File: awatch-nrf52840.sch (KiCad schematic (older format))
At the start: 24 parts, among them U1 nRF52840, X1 ABM11W-32.0000MHZ-8-B1U-T3

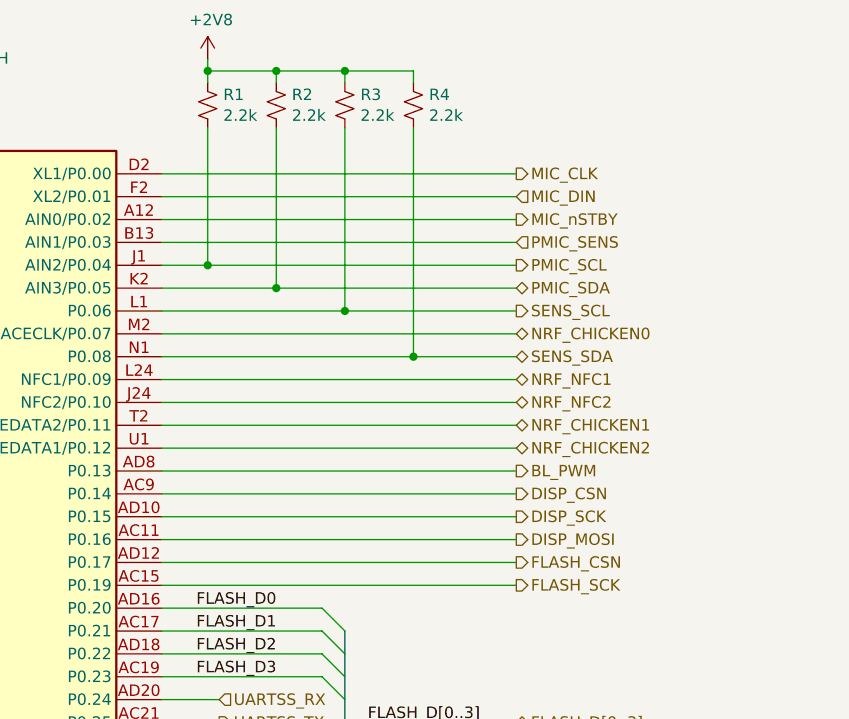
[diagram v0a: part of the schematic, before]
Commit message: route NFC
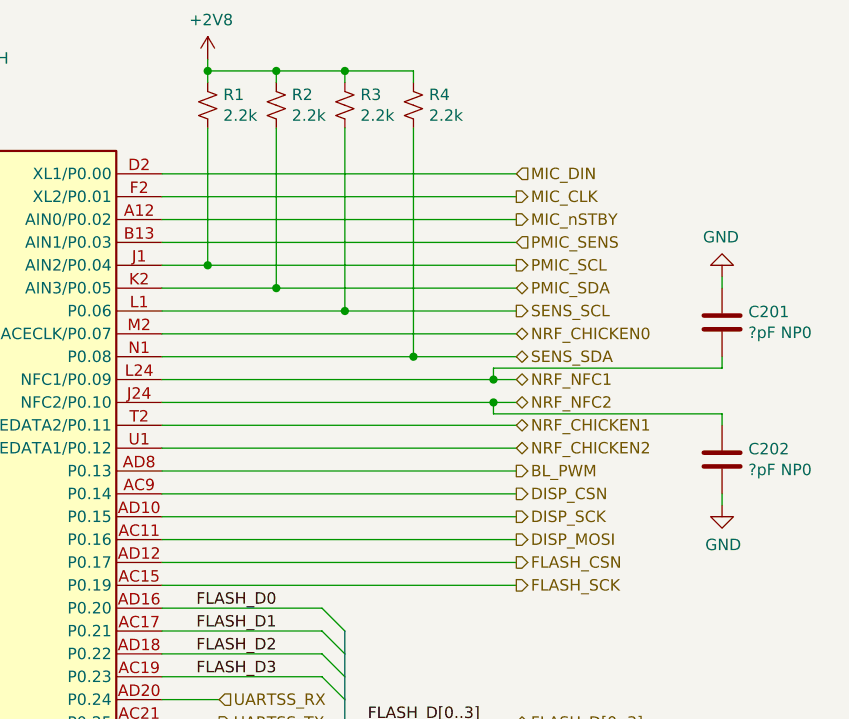
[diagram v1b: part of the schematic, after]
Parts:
- added C201, C202: ?pF NP0, Capacitor_SMD:C_0603_1608Metric, symbol Device:C
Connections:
- net GND: now also C201.1, C202.2
- net MIC_CLK: now also U1.F2 (XL2/P0.01); no longer U1.D2 (XL1/P0.00)
- net MIC_DIN: now also U1.D2 (XL1/P0.00); no longer U1.F2 (XL2/P0.01)
- net NRF_NFC1: now also C201.2
- net NRF_NFC2: now also C202.1
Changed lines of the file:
@@
 Wire Wire Line
 	6700 2100 5150 2100
-Text HLabel 6700 2000 2    50   Output ~ 0
+Text HLabel 6700 2100 2    50   Output ~ 0
 MIC_CLK
-Text HLabel 6700 2100 2    50   Input ~ 0
+Text HLabel 6700 2000 2    50   Input ~ 0
 MIC_DIN
 Text HLabel 6700 2200 2    50   Output ~ 0
@@
 NRF_NFC2
 Wire Wire Line
-	6700 3000 5150 3000
-Wire Wire Line
-	5150 2900 6700 2900
+	6700 3000 6600 3000
+Wire Wire Line
+	5150 2900 6600 2900
 Text HLabel 6700 2700 2    50   BiDi ~ 0
 NRF_CHICKEN0
@@
 	1900 2700 2050 2700
 $Comp
-L power:GND #PWR?
+L power:GND #PWR0141
 U 1 1 5C322A37
 P 1900 3100
-F 0 "#PWR?" H 1900 2850 50  0001 C CNN
+F 0 "#PWR0141" H 1900 2850 50  0001 C CNN
 F 1 "GND" H 1905 2927 50  0000 C CNN
 F 2 "" H 1900 3100 50  0001 C CNN
@@
 Wire Wire Line
 	1900 3000 1900 3100
+$Comp
+L Device:C C201
+U 1 1 5C3ACC54
+P 7600 2650
+F 0 "C201" H 7715 2696 50  0000 L CNN
+F 1 "?pF NP0" H 7715 2605 50  0000 L CNN
+F 2 "Capacitor_SMD:C_0603_1608Metric" H 7638 2500 50  0001 C CNN
+F 3 "~" H 7600 2650 50  0001 C CNN
+	1    7600 2650
+	1    0    0    -1
+$EndComp
+$Comp
+L Device:C C202
+U 1 1 5C3ACCC4
+P 7600 3250
+F 0 "C202" H 7715 3296 50  0000 L CNN
+F 1 "?pF NP0" H 7715 3205 50  0000 L CNN
+F 2 "Capacitor_SMD:C_0603_1608Metric" H 7638 3100 50  0001 C CNN
+F 3 "~" H 7600 3250 50  0001 C CNN
+	1    7600 3250
+	1    0    0    -1
+$EndComp
+Wire Wire Line
+	6600 2900 6600 2850
+Wire Wire Line
+	6600 2850 7600 2850
+Connection ~ 6600 2900
+Wire Wire Line
+	6600 2900 6700 2900
+Wire Wire Line
+	6600 3000 6600 3050
+Wire Wire Line
+	6600 3050 7600 3050
+Connection ~ 6600 3000
+Wire Wire Line
+	6600 3000 5150 3000
+$Comp
+L power:GND #PWR0209
+U 1 1 5C3B6652
+P 7600 3450
+F 0 "#PWR0209" H 7600 3200 50  0001 C CNN
+F 1 "GND" H 7605 3277 50  0000 C CNN
+F 2 "" H 7600 3450 50  0001 C CNN
+F 3 "" H 7600 3450 50  0001 C CNN
+	1    7600 3450
+	1    0    0    -1
+$EndComp
+$Comp
+L power:GND #PWR0208
+U 1 1 5C3BB5DC
+P 7600 2450
+F 0 "#PWR0208" H 7600 2200 50  0001 C CNN
+F 1 "GND" H 7605 2277 50  0000 C CNN
+F 2 "" H 7600 2450 50  0001 C CNN
+F 3 "" H 7600 2450 50  0001 C CNN
+	1    7600 2450
+	-1   0    0    1
+$EndComp
+Wire Wire Line
+	7600 3400 7600 3450
+Wire Wire Line
+	7600 3100 7600 3050
+Wire Wire Line
+	7600 2450 7600 2500
+Wire Wire Line
+	7600 2800 7600 2850
 Wire Bus Line
 	5950 4000 5950 4400

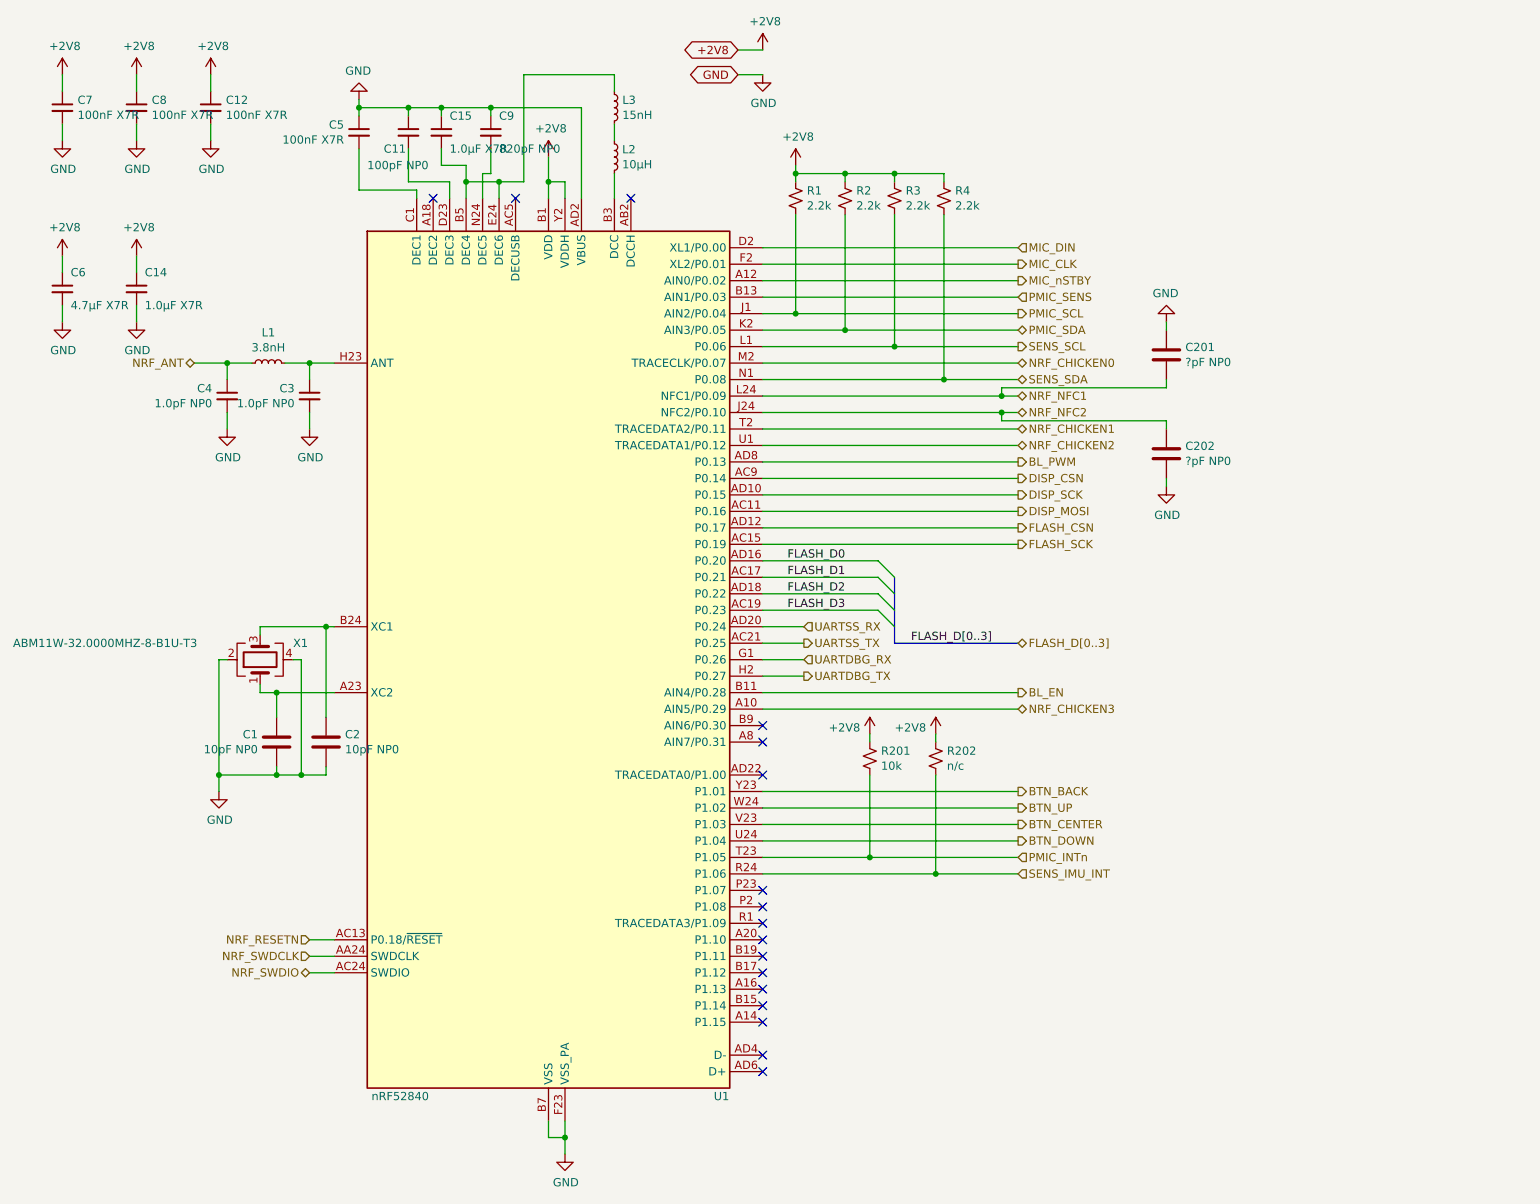
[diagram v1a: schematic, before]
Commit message: nRF pinout changes for routability
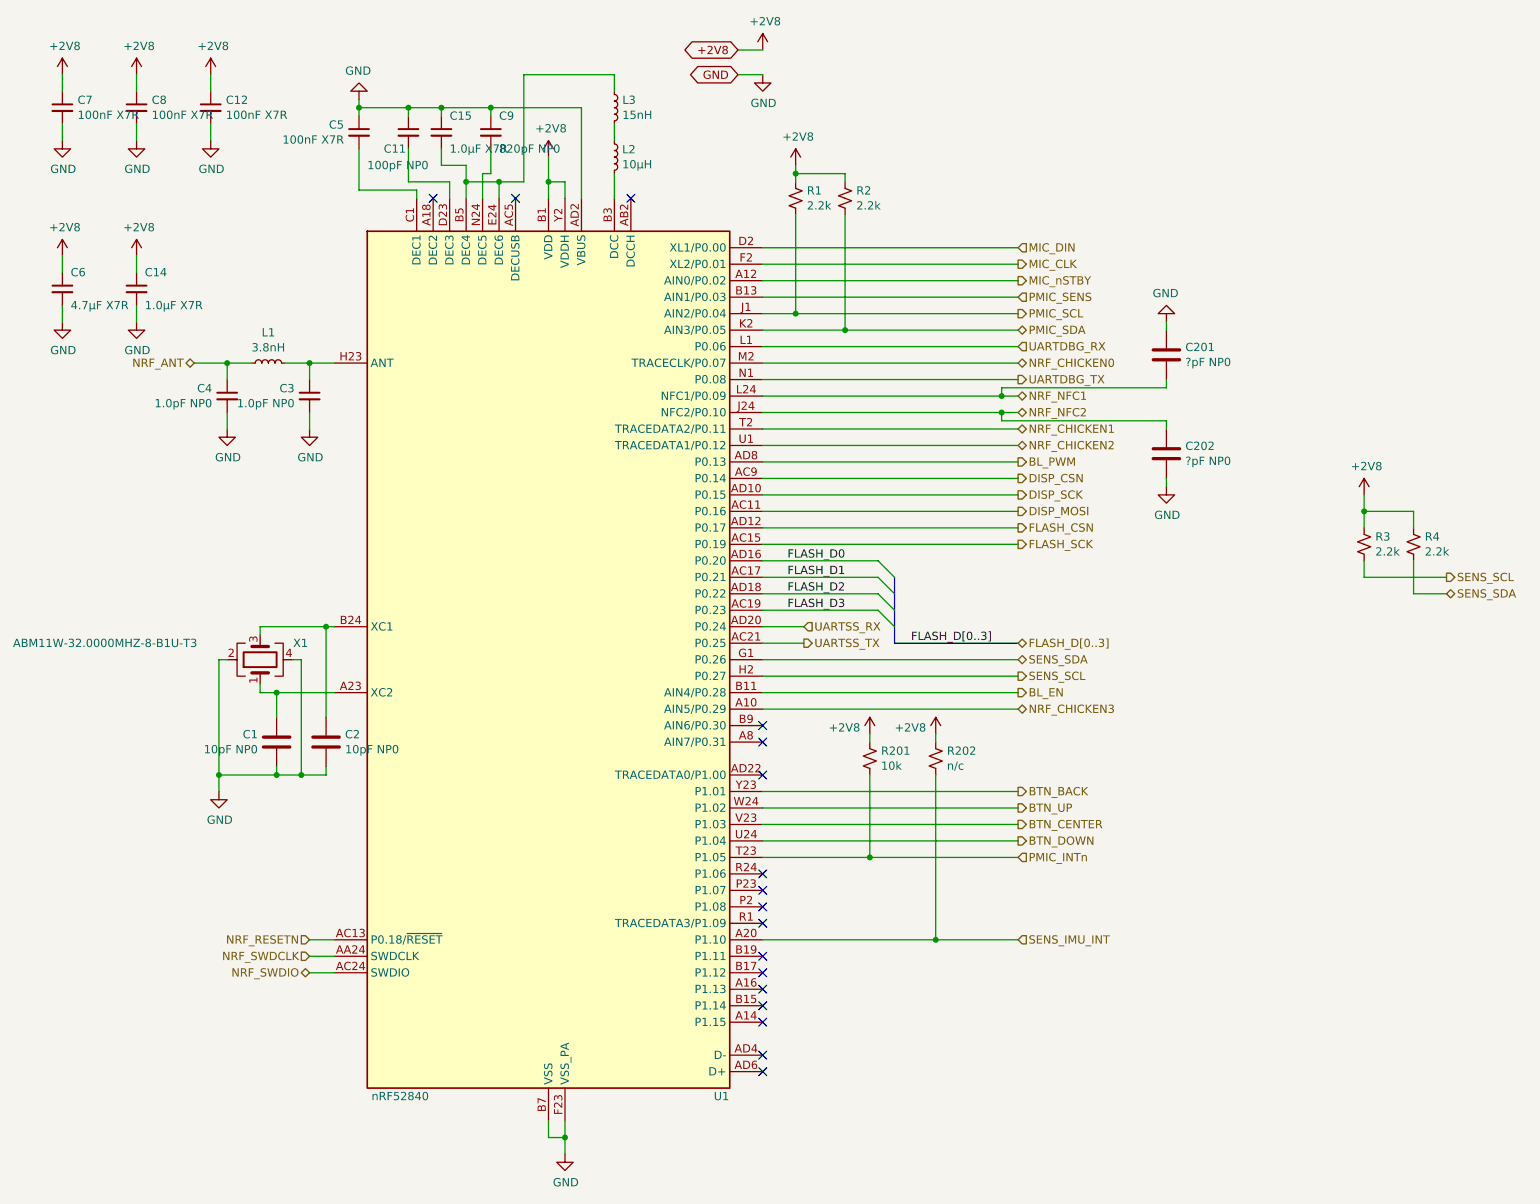
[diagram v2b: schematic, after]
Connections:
- net SENS_IMU_INT: now also U1.A20 (P1.10); no longer U1.R24 (P1.06)
- net SENS_SCL: now also U1.H2 (P0.27); no longer U1.L1 (P0.06)
- net SENS_SDA: now also U1.G1 (P0.26); no longer U1.N1 (P0.08)
- net UARTDBG_RX: now also U1.L1 (P0.06); no longer U1.G1 (P0.26)
- net UARTDBG_TX: now also U1.N1 (P0.08); no longer U1.H2 (P0.27)
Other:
- moved on the sheet: R3, R4
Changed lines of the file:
@@
 Text HLabel 5400 4400 2    50   Output ~ 0
 UARTSS_TX
-Text HLabel 5400 4500 2    50   Input ~ 0
+Text HLabel 6700 2600 2    50   Input ~ 0
 UARTDBG_RX
-Text HLabel 5400 4600 2    50   Output ~ 0
+Text HLabel 6700 2800 2    50   Output ~ 0
 UARTDBG_TX
-Wire Wire Line
-	5400 4600 5150 4600
-Wire Wire Line
-	5150 4500 5400 4500
 Wire Wire Line
 	5400 4400 5150 4400
@@
 Wire Wire Line
 	6700 4700 5150 4700
-Text HLabel 6700 2600 2    50   Output ~ 0
+Text HLabel 6700 4600 2    50   Output ~ 0
 SENS_SCL
-Text HLabel 6700 2800 2    50   BiDi ~ 0
+Text HLabel 6700 4500 2    50   BiDi ~ 0
 SENS_SDA
 Wire Wire Line
-	6700 2600 5950 2600
-Wire Wire Line
-	6700 2800 6250 2800
-Wire Wire Line
 	6700 5300 5150 5300
-Wire Wire Line
-	6700 5600 5150 5600
 Wire Wire Line
 	5150 5500 6700 5500
@@
 L Device:R_Small_US R3
 U 1 1 5C2F1FF1
-P 5950 1700
-F 0 "R3" H 6018 1746 50  0000 L CNN
-F 1 "2.2k" H 6018 1655 50  0000 L CNN
-F 2 "Resistor_SMD:R_0603_1608Metric" H 5950 1700 50  0001 C CNN
-F 3 "~" H 5950 1700 50  0001 C CNN
-	1    5950 1700
+P 8800 3800
+F 0 "R3" H 8868 3846 50  0000 L CNN
+F 1 "2.2k" H 8868 3755 50  0000 L CNN
+F 2 "Resistor_SMD:R_0603_1608Metric" H 8800 3800 50  0001 C CNN
+F 3 "~" H 8800 3800 50  0001 C CNN
+	1    8800 3800
 	1    0    0    -1
 $EndComp
@@
 L Device:R_Small_US R4
 U 1 1 5C2F202B
-P 6250 1700
-F 0 "R4" H 6318 1746 50  0000 L CNN
-F 1 "2.2k" H 6318 1655 50  0000 L CNN
-F 2 "Resistor_SMD:R_0603_1608Metric" H 6250 1700 50  0001 C CNN
-F 3 "~" H 6250 1700 50  0001 C CNN
-	1    6250 1700
+P 9100 3800
+F 0 "R4" H 9168 3846 50  0000 L CNN
+F 1 "2.2k" H 9168 3755 50  0000 L CNN
+F 2 "Resistor_SMD:R_0603_1608Metric" H 9100 3800 50  0001 C CNN
+F 3 "~" H 9100 3800 50  0001 C CNN
+	1    9100 3800
 	1    0    0    -1
 $EndComp
@@
 Wire Wire Line
 	5650 2500 6700 2500
-Wire Wire Line
-	5950 1800 5950 2600
-Connection ~ 5950 2600
-Wire Wire Line
-	5950 2600 5150 2600
-Wire Wire Line
-	6250 1800 6250 2800
-Connection ~ 6250 2800
-Wire Wire Line
-	6250 2800 5150 2800
 $Comp
 L power:+2V8 #PWR0118
@@
 Wire Wire Line
 	5350 1550 5350 1600
-Wire Wire Line
-	5650 1550 5950 1550
-Wire Wire Line
-	5950 1550 5950 1600
-Connection ~ 5650 1550
-Wire Wire Line
-	5950 1550 6250 1550
-Wire Wire Line
-	6250 1550 6250 1600
-Connection ~ 5950 1550
 NoConn ~ 5150 4900
 NoConn ~ 5150 5000
@@
 NoConn ~ 5150 5900
 NoConn ~ 5150 6000
-NoConn ~ 5150 6200
+NoConn ~ 5150 5800
 NoConn ~ 5150 6100
 NoConn ~ 5150 6300
@@
 Wire Wire Line
 	5800 4950 5800 5000
-Text HLabel 6700 5800 2    50   Input ~ 0
+Text HLabel 6700 6200 2    50   Input ~ 0
 SENS_IMU_INT
-Wire Wire Line
-	5150 5800 6200 5800
 $Comp
 L Device:R_Small_US R202
@@
 Wire Wire Line
 	6200 4950 6200 5000
-Wire Wire Line
-	6200 5200 6200 5800
-Connection ~ 6200 5800
-Wire Wire Line
-	6200 5800 6700 5800
 Wire Wire Line
 	4050 1700 4050 1150
@@
 Wire Wire Line
 	7600 2800 7600 2850
+Wire Wire Line
+	5150 5600 6700 5600
+Wire Wire Line
+	5150 6200 6200 6200
+Wire Wire Line
+	6200 5200 6200 6200
+Connection ~ 6200 6200
+Wire Wire Line
+	6200 6200 6700 6200
+Text HLabel 9300 4000 2    50   Output ~ 0
+SENS_SCL
+Text HLabel 9300 4100 2    50   BiDi ~ 0
+SENS_SDA
+Wire Wire Line
+	9100 3900 9100 4100
+Wire Wire Line
+	9100 4100 9300 4100
+Wire Wire Line
+	9300 4000 8800 4000
+Wire Wire Line
+	8800 4000 8800 3900
+Wire Wire Line
+	8800 3700 8800 3600
+Wire Wire Line
+	8800 3600 9100 3600
+Wire Wire Line
+	9100 3600 9100 3700
+$Comp
+L power:+2V8 #PWR0145
+U 1 1 5C4096C0
+P 8800 3500
+F 0 "#PWR0145" H 8800 3350 50  0001 C CNN
+F 1 "+2V8" H 8815 3673 50  0000 C CNN
+F 2 "" H 8800 3500 50  0001 C CNN
+F 3 "" H 8800 3500 50  0001 C CNN
+	1    8800 3500
+	1    0    0    -1
+$EndComp
+Wire Wire Line
+	8800 3500 8800 3600
+Connection ~ 8800 3600
+Wire Wire Line
+	5150 2600 6700 2600
+Wire Wire Line
+	5150 2800 6700 2800
+Wire Wire Line
+	5150 4500 6700 4500
+Wire Wire Line
+	5150 4600 6700 4600
 Wire Bus Line
 	5950 4000 5950 4400

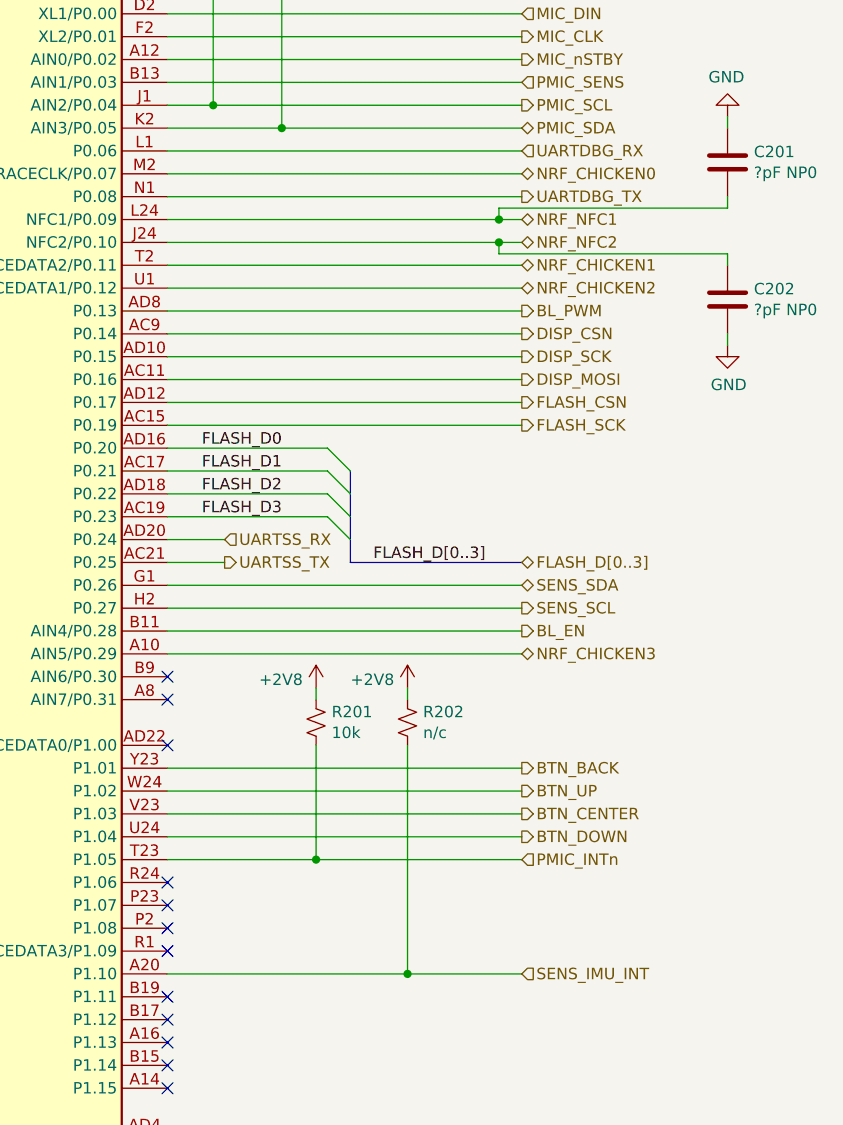
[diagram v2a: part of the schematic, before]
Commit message: some PMIC and sensor routing
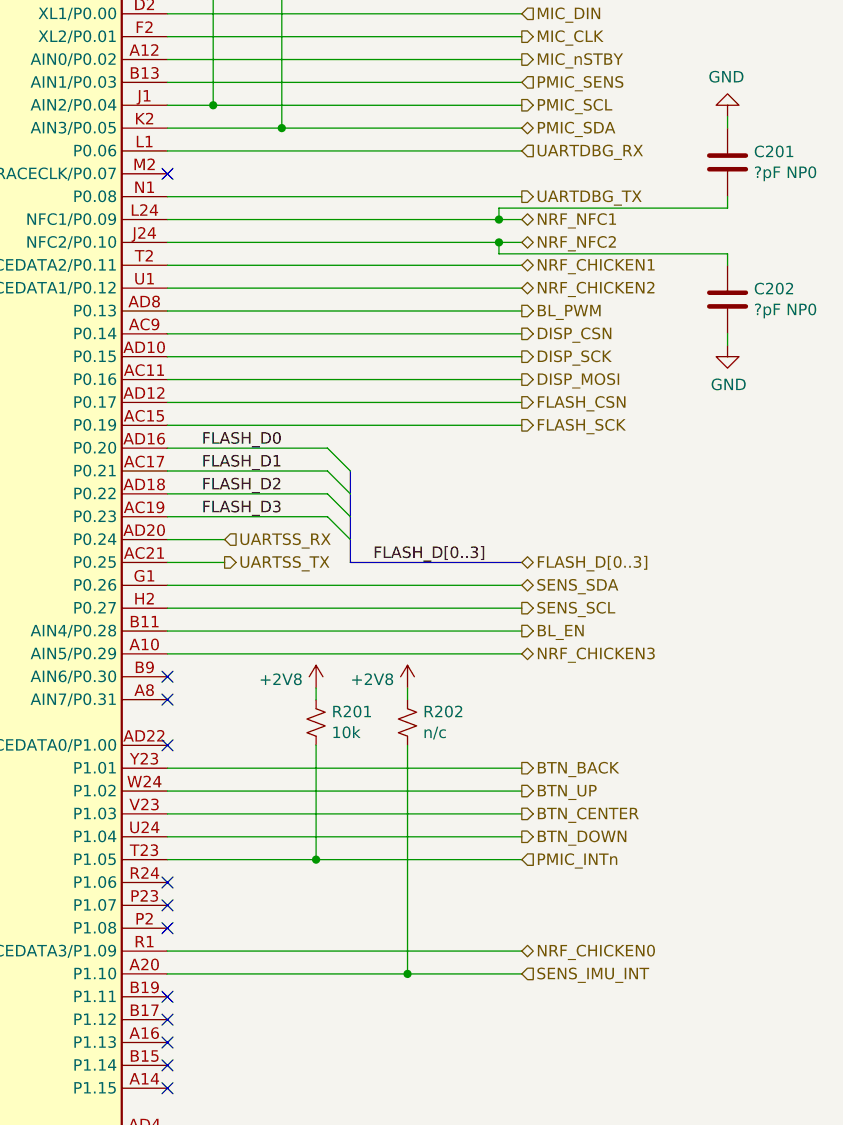
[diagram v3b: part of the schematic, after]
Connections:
- net NRF_CHICKEN0: now also U1.R1 (TRACEDATA3/P1.09); no longer U1.M2 (TRACECLK/P0.07)
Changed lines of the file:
@@
 Wire Wire Line
 	5150 2900 6600 2900
-Text HLabel 6700 2700 2    50   BiDi ~ 0
+Text HLabel 6700 6100 2    50   BiDi ~ 0
 NRF_CHICKEN0
 Text HLabel 6700 3100 2    50   BiDi ~ 0
@@
 NRF_CHICKEN2
 Wire Wire Line
-	6700 2700 5150 2700
+	6700 6100 5150 6100
 Wire Wire Line
 	5150 3100 6700 3100
@@
 NoConn ~ 5150 6000
 NoConn ~ 5150 5800
-NoConn ~ 5150 6100
+NoConn ~ 5150 2700
 NoConn ~ 5150 6300
 NoConn ~ 5150 6400
